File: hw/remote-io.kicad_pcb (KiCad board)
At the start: 2 copper layers, 62 parts, among them P1 CONN_01X02, P2 CONN_01X08, P3 CONN_01X08, P4 CONN_02X20, P5 CONN_01X08, P6 CONN_01X04, P7 CONN_01X02, Q1 DMG2305UX, Q2 DMMT5401, U1 AP1506, U2 MCP3008, U3 CAT24C32, U4 MAX3488

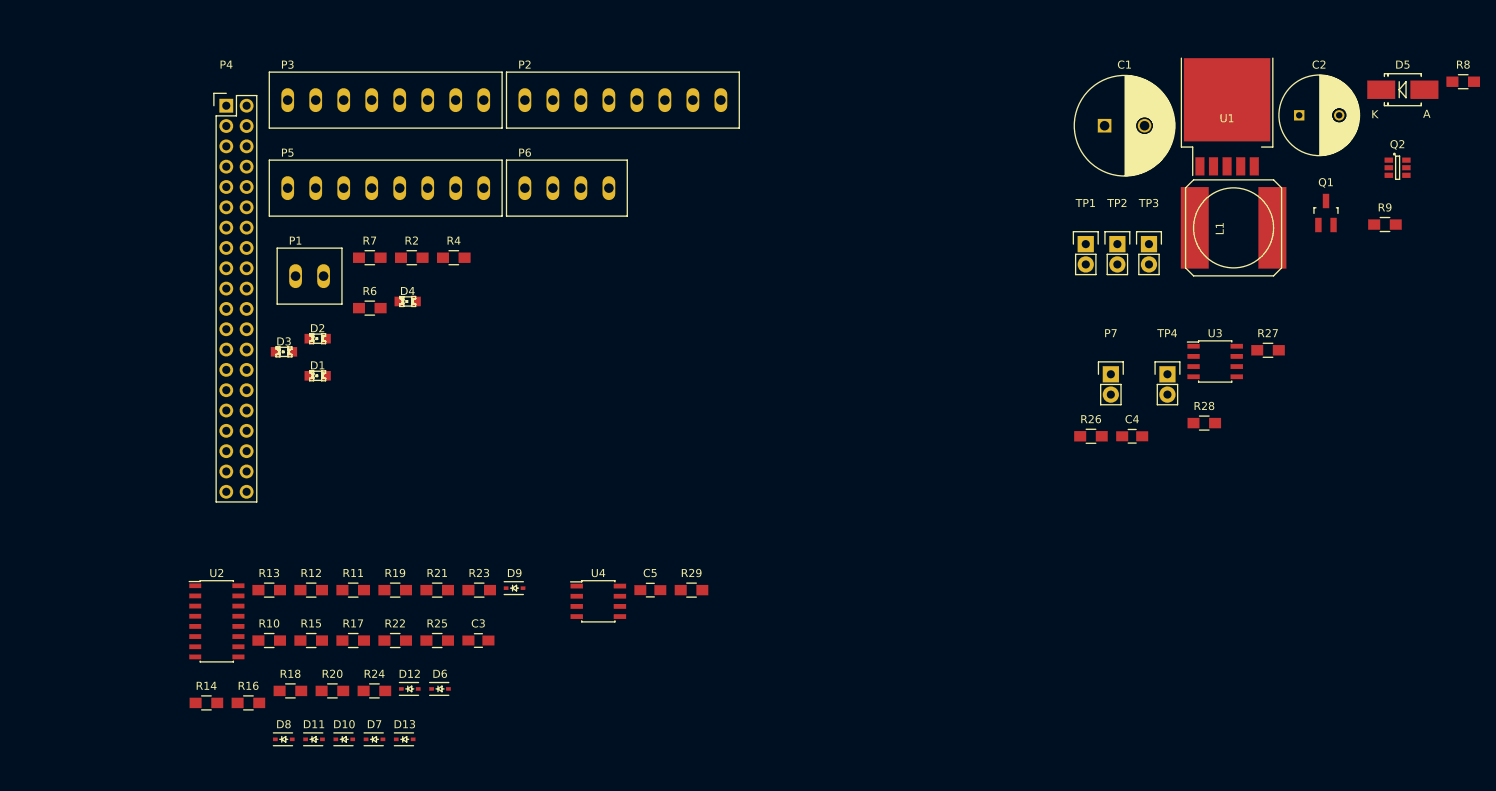
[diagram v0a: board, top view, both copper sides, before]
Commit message: added CAN power, controller, and transceiver to schem and updated PCB
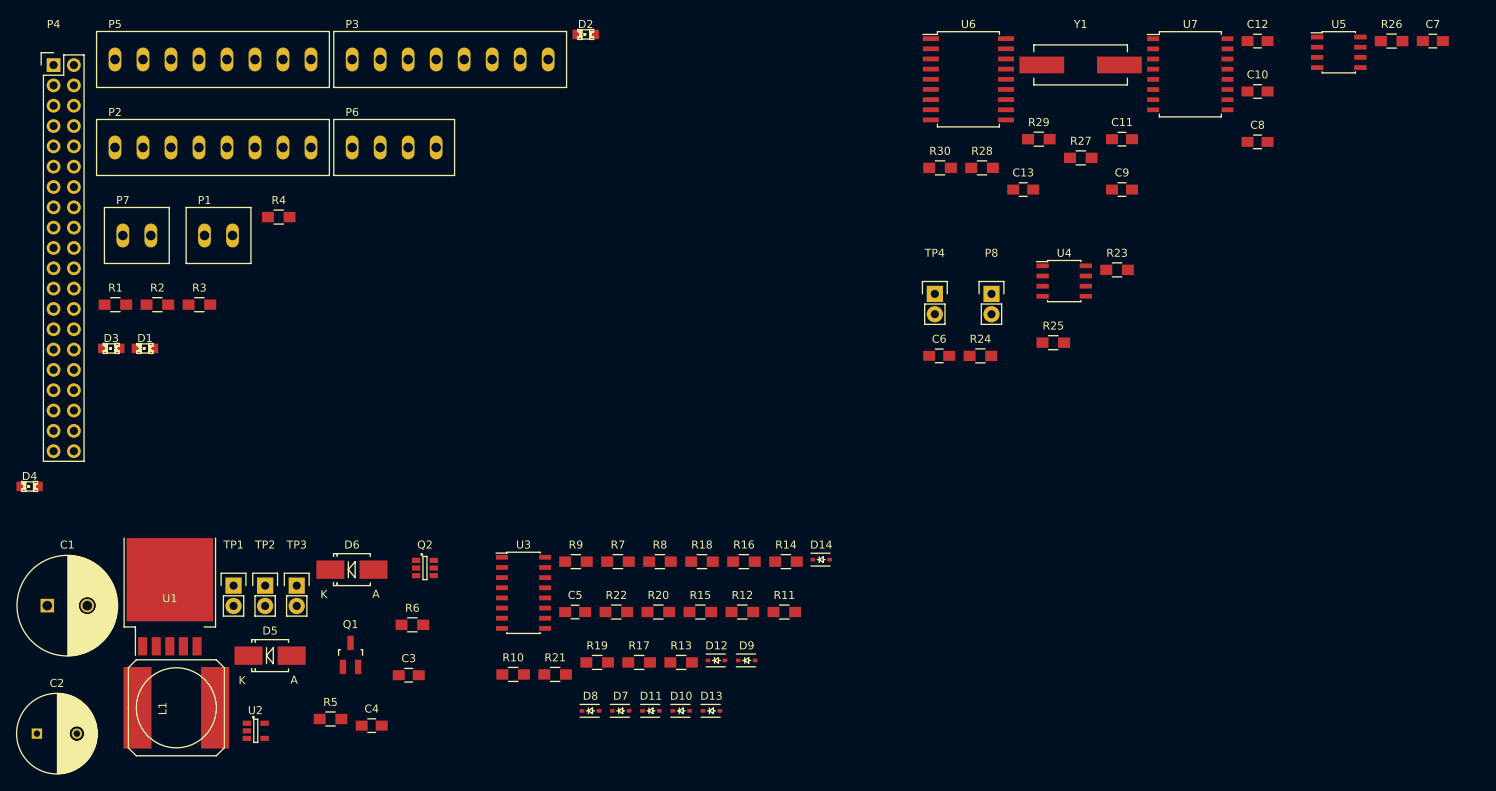
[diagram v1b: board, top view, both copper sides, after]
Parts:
- added C10: 18pF, Capacitors_SMD:C_0805_HandSoldering, F.Cu at (220.4, 52.7)
- added C11: 18pF, Capacitors_SMD:C_0805_HandSoldering, F.Cu at (203.4, 58.7)
- added C12: 0.1uF, Capacitors_SMD:C_0805_HandSoldering, F.Cu at (220.4, 46.4)
- added C13: 0.1uF, Capacitors_SMD:C_0805_HandSoldering, F.Cu at (191.1, 65.0)
- added C6: 0.1uF, Capacitors_SMD:C_0805_HandSoldering, F.Cu at (180.6, 85.8)
- added C7: 0.1uF, Capacitors_SMD:C_0805_HandSoldering, F.Cu at (242.3, 46.4)
- added C8: 0.1uF, Capacitors_SMD:C_0805_HandSoldering, F.Cu at (220.4, 59.0)
- added C9: 0.1uF, Capacitors_SMD:C_0805_HandSoldering, F.Cu at (203.4, 65.0)
- added D14: 3.9V, Diodes_SMD:SOD-323, F.Cu at (165.8, 111.2)
- added P8: CONN_01X02, Pin_Headers:Pin_Header_Straight_1x02, F.Cu at (187.1, 78.0)
- added R1: 65, Resistors_SMD:R_0805_HandSoldering, F.Cu at (77.6, 79.4)
- added R3: 65, Resistors_SMD:R_0805_HandSoldering, F.Cu at (88.1, 79.4)
- added R30: 60, Resistors_SMD:R_0805_HandSoldering, F.Cu at (180.7, 62.3)
- added R5: 10k, Resistors_SMD:R_0805_HandSoldering, F.Cu at (104.5, 131.1)
- added U5: MAX3488, Housings_SOIC:SOIC-8_3.9x4.9mm_Pitch1.27mm, F.Cu at (230.5, 47.8)
- added U6: MCP2515, Housings_SOIC:SOIC-18_7.5x11.6mm_Pitch1.27mm, F.Cu at (184.2, 51.2)
- added U7: ADM3054, Housings_SOIC:SOIC-16_7.5x10.3mm_Pitch1.27mm, F.Cu at (212.0, 50.6)
- added Y1: Crystal, Crystals:Crystal_HC49-SD_SMD, F.Cu at (198.3, 49.4)
- C3, C4: value 0.1uF -> 10uF
- D6: value 3.9V -> D_Schottky; footprint Diodes_SMD:SOD-323 -> Diodes_SMD:Diode-SMB_Handsoldering
- P7: footprint Pin_Headers:Pin_Header_Straight_1x02 -> remote-io:OSTTE020104
- R11, R12, R13, R19, R20, R21: value 78.7k -> 11.3k
- R15, R16, R17: value 11.3k -> 78.7k
- R23, R24: value 11.3k -> 3.9k
- R25: value 11.3k -> 1k
- R26: value 3.9k -> 120
- R27: value 3.9k -> 4.7K
- R28: value 1k -> 4.7K
- R29: value 120 -> 60
- R6: value 65 -> 47k
- R7: value 65 -> 78.7k
- R8: value 10k -> 78.7k
- R9: value 47k -> 78.7k
- U2: value MCP3008 -> LP2992; footprint Housings_SOIC:SOIC-16_3.9x9.9mm_Pitch1.27mm -> Housings_SOT-23_SOT-143_TSOT-6:SOT-23-5
- U3: value CAT24C32 -> MCP3008; footprint Housings_SOIC:SOIC-8_3.9x4.9mm_Pitch1.27mm -> Housings_SOIC:SOIC-16_3.9x9.9mm_Pitch1.27mm
- U4: value MAX3488 -> CAT24C32
- moved C2 175.7 mm to (67.8, 133.0)
- moved D5 158.3 mm to (96.9, 123.2)
- moved L1 145.1 mm to (85.2, 129.7)
- moved C1 145.1 mm to (69.1, 117.0)
- moved U1 145.1 mm to (84.4, 122.1)
- moved Q1 133.9 mm to (107.0, 123.1)
- moved Q2 131.5 mm to (116.3, 112.3)
- moved P7 124.7 mm to (78.5, 70.7)
- moved R8 117.0 mm to (145.7, 111.5)
- moved TP1 114.8 mm to (92.4, 114.5)
- moved TP3 114.8 mm to (100.3, 114.5)
- moved TP2 114.8 mm to (96.3, 114.5)
- moved R9 109.6 mm to (135.2, 111.5)
- moved C4 101.7 mm to (109.6, 132.0)
- moved U3 91.2 mm to (128.6, 115.4)
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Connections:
- C3 pad 1: +3V3 -> Net-(C3-Pad1)
- C3 pad 2: GND -> Net-(C3-Pad2)
- C4 pad 1: +3V3 -> Net-(C4-Pad1)
- C4 pad 2: GND -> Net-(C3-Pad2)
- D10 pad 1: /Battery Monitor/ADC_IN4 -> /Battery Monitor/ADC_IN3
- D11 pad 1: /Battery Monitor/ADC_IN5 -> /Battery Monitor/ADC_IN4
- D12 pad 1: /Battery Monitor/ADC_IN6 -> /Battery Monitor/ADC_IN5
- D13 pad 1: /Battery Monitor/ADC_IN7 -> /Battery Monitor/ADC_IN6
- D6 pad 1: /Battery Monitor/ADC_IN0 -> +12V
- D6 pad 2: Net-(D6-Pad2) -> Net-(C3-Pad1)
- D7 pad 1: /Battery Monitor/ADC_IN1 -> /Battery Monitor/ADC_IN0
- D8 pad 1: /Battery Monitor/ADC_IN2 -> /Battery Monitor/ADC_IN1
- D9 pad 1: /Battery Monitor/ADC_IN3 -> /Battery Monitor/ADC_IN2
- P4 pad 26: Net-(P4-Pad26) -> /CAN Controller and Transceiver/CAN_~CS
- P4 pad 5: Net-(P4-Pad5) -> /CAN Controller and Transceiver/CAN_VSENSE
- P4 pad 7: Net-(P4-Pad7) -> /CAN Controller and Transceiver/CAN_~INT
- P7 pad 1: Net-(P7-Pad1) -> /CAN Controller and Transceiver/CAN_H
- P7 pad 2: Net-(P7-Pad2) -> /CAN Controller and Transceiver/CAN_L
- R10 pad 1: /Battery Monitor/BAT_MEAS0 -> /Battery Monitor/BAT_MEAS3
- R10 pad 2: /Battery Monitor/ADC_IN0 -> /Battery Monitor/ADC_IN3
- R11 pad 1: /Battery Monitor/BAT_MEAS1 -> /Battery Monitor/ADC_IN0
- R11 pad 2: /Battery Monitor/ADC_IN1 -> Net-(D7-Pad2)
- R12 pad 1: /Battery Monitor/BAT_MEAS2 -> /Battery Monitor/ADC_IN1
- R12 pad 2: /Battery Monitor/ADC_IN2 -> Net-(D8-Pad2)
- R13 pad 1: /Battery Monitor/BAT_MEAS3 -> /Battery Monitor/ADC_IN2
- R13 pad 2: /Battery Monitor/ADC_IN3 -> Net-(D9-Pad2)
- R14 pad 1: /Battery Monitor/ADC_IN0 -> /Battery Monitor/ADC_IN3
- R14 pad 2: Net-(D6-Pad2) -> Net-(D10-Pad2)
- R15 pad 1: /Battery Monitor/ADC_IN1 -> /Battery Monitor/BAT_MEAS4
- R15 pad 2: Net-(D7-Pad2) -> /Battery Monitor/ADC_IN4
- R16 pad 1: /Battery Monitor/ADC_IN2 -> /Battery Monitor/BAT_MEAS5
- R16 pad 2: Net-(D8-Pad2) -> /Battery Monitor/ADC_IN5
- R17 pad 1: /Battery Monitor/ADC_IN3 -> /Battery Monitor/BAT_MEAS6
- R17 pad 2: Net-(D9-Pad2) -> /Battery Monitor/ADC_IN6
- R18 pad 1: /Battery Monitor/BAT_MEAS4 -> /Battery Monitor/BAT_MEAS7
- R18 pad 2: /Battery Monitor/ADC_IN4 -> /Battery Monitor/ADC_IN7
- R19 pad 1: /Battery Monitor/BAT_MEAS5 -> /Battery Monitor/ADC_IN4
- R19 pad 2: /Battery Monitor/ADC_IN5 -> Net-(D11-Pad2)
- R2 pad 1: /LED0 -> /LED1
- R2 pad 2: Net-(D1-Pad2) -> Net-(D2-Pad2)
- R20 pad 1: /Battery Monitor/BAT_MEAS6 -> /Battery Monitor/ADC_IN5
- R20 pad 2: /Battery Monitor/ADC_IN6 -> Net-(D12-Pad2)
- R21 pad 1: /Battery Monitor/BAT_MEAS7 -> /Battery Monitor/ADC_IN6
- R21 pad 2: /Battery Monitor/ADC_IN7 -> Net-(D13-Pad2)
- R22 pad 1: /Battery Monitor/ADC_IN4 -> /Battery Monitor/ADC_IN7
- R22 pad 2: Net-(D10-Pad2) -> Net-(D14-Pad2)
- R23 pad 1: /Battery Monitor/ADC_IN5 -> /I2C ID EEPROM/ID_SC
- R23 pad 2: Net-(D11-Pad2) -> +3V3
- R24 pad 1: /Battery Monitor/ADC_IN6 -> /I2C ID EEPROM/ID_SD
- R24 pad 2: Net-(D12-Pad2) -> +3V3
- R25 pad 1: /Battery Monitor/ADC_IN7 -> +3V3
- R25 pad 2: Net-(D13-Pad2) -> Net-(P8-Pad1)
- R26 pad 1: /I2C ID EEPROM/ID_SC -> /RS-422 Level Converter/RS422_GPS
- R26 pad 2: +3V3 -> /RS-422 Level Converter/~RS422_GPS
- R27 pad 1: /I2C ID EEPROM/ID_SD -> /CAN Controller and Transceiver/CAN_~INT
- R28 pad 1: +3V3 -> Net-(R28-Pad1)
- R28 pad 2: Net-(P7-Pad1) -> +3V3
- R29 pad 1: /RS-422 Level Converter/RS422_GPS -> /CAN Controller and Transceiver/CAN_H
- R29 pad 2: /RS-422 Level Converter/~RS422_GPS -> Net-(C13-Pad1)
- R4 pad 1: /LED1 -> /LED3
- R4 pad 2: Net-(D2-Pad2) -> Net-(D4-Pad2)
- R6 pad 1: /LED2 -> /Power/V_GATE
- R6 pad 2: Net-(D3-Pad2) -> Net-(R5-Pad2)
- R7 pad 1: /LED3 -> /Battery Monitor/BAT_MEAS0
- R7 pad 2: Net-(D4-Pad2) -> /Battery Monitor/ADC_IN0
- R8 pad 1: /Power/V_BASES -> /Battery Monitor/BAT_MEAS1
- R8 pad 2: Net-(R8-Pad2) -> /Battery Monitor/ADC_IN1
- R9 pad 1: /Power/V_GATE -> /Battery Monitor/BAT_MEAS2
- R9 pad 2: Net-(R8-Pad2) -> /Battery Monitor/ADC_IN2
- TP4 pad 1: Net-(P7-Pad1) -> Net-(P8-Pad1)
- TP4 pad 2: Net-(P7-Pad2) -> Net-(P8-Pad2)
- U2 pad 1: /Battery Monitor/ADC_IN0 -> +12V
- U2 pad 2: /Battery Monitor/ADC_IN1 -> GND
- U2 pad 3: /Battery Monitor/ADC_IN2 -> +12V
- U2 pad 4: /Battery Monitor/ADC_IN3 -> Net-(C4-Pad1)
- U2 pad 5: /Battery Monitor/ADC_IN4 -> Net-(C3-Pad1)
- U3 pad 1: GND -> /Battery Monitor/ADC_IN0
- U3 pad 2: GND -> /Battery Monitor/ADC_IN1
- U3 pad 3: GND -> /Battery Monitor/ADC_IN2
- U3 pad 4: GND -> /Battery Monitor/ADC_IN3
- U3 pad 5: /I2C ID EEPROM/ID_SD -> /Battery Monitor/ADC_IN4
- U3 pad 6: /I2C ID EEPROM/ID_SC -> /Battery Monitor/ADC_IN5
- U3 pad 7: Net-(P7-Pad1) -> /Battery Monitor/ADC_IN6
- U3 pad 8: +3V3 -> /Battery Monitor/ADC_IN7
- U4 pad 1: +3V3 -> GND
- U4 pad 2: /RS-422 Level Converter/RX_GPS -> GND
- U4 pad 5: Net-(U4-Pad5) -> /I2C ID EEPROM/ID_SD
- U4 pad 6: Net-(U4-Pad6) -> /I2C ID EEPROM/ID_SC
- U4 pad 7: /RS-422 Level Converter/~RS422_GPS -> Net-(P8-Pad1)
- U4 pad 8: /RS-422 Level Converter/RS422_GPS -> +3V3
